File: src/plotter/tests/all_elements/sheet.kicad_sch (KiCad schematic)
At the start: 1 part, among them U1 TL072

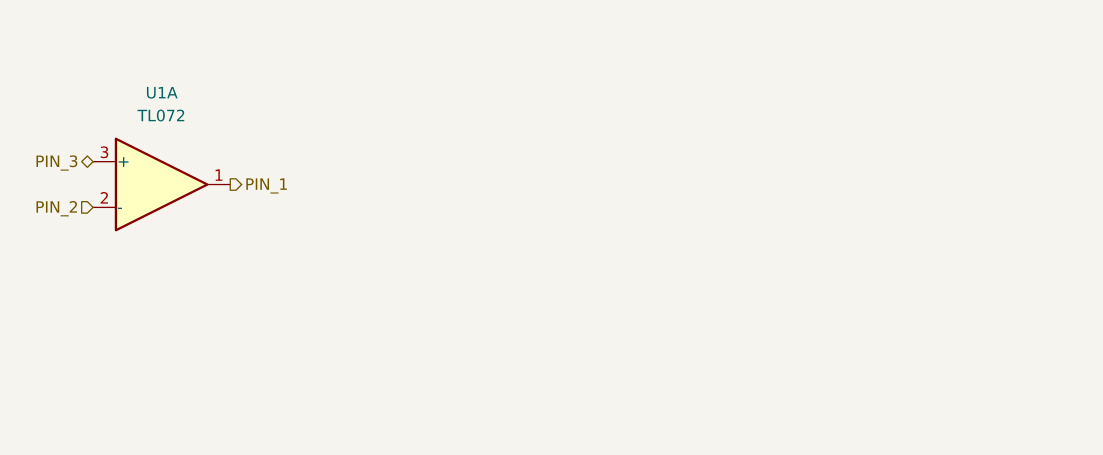
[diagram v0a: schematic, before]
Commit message: update draw arc in plotter and work on docs
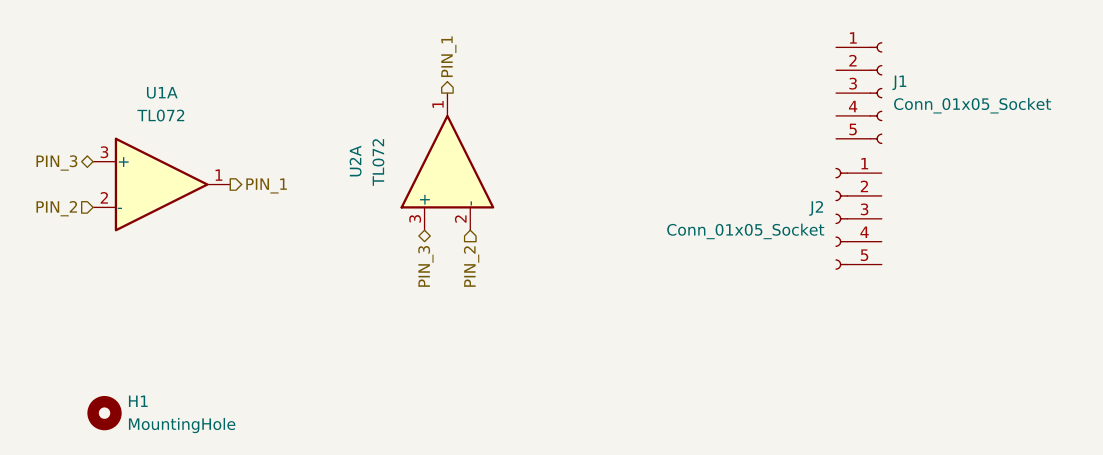
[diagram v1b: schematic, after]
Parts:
- added H1: MountingHole, symbol Mechanical:MountingHole
- added J1, J2: Conn_01x05_Socket, symbol Connector:Conn_01x05_Socket
- added U2: TL072, symbol Amplifier_Operational:TL072
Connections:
- net PIN_1: now also U2.1
- net PIN_2: now also U2.2 (-)
- net PIN_3: now also U2.3 (+)
